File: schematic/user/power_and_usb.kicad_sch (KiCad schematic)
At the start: 27 parts, among them J1 TYPE-C-31-M-04, Q1 AO3401A, Q2 AO3401A, Q5 MBT3904DW1T1, U1 TP4056, U2 MAX17048G+T10, U3 TLV1117LV-33

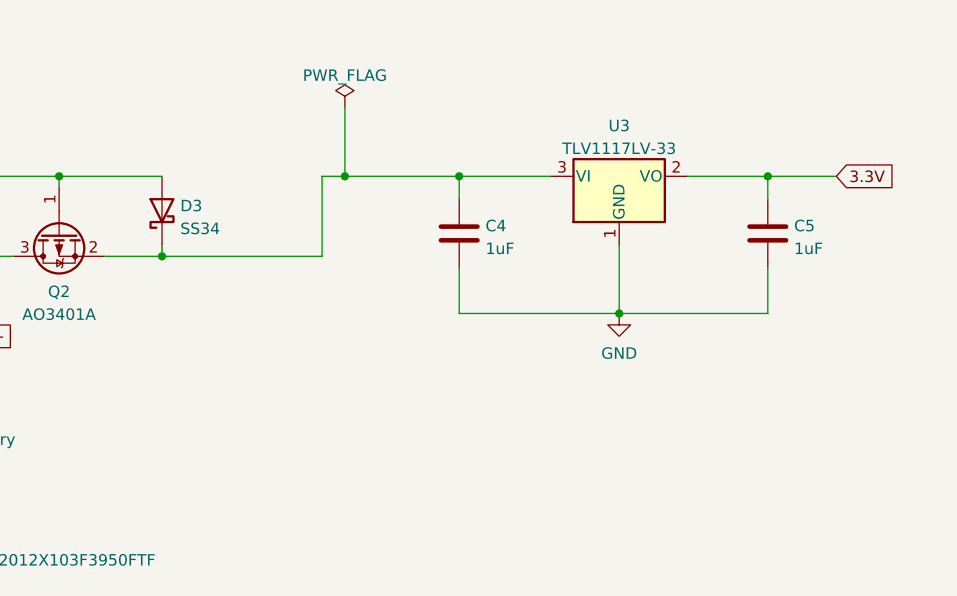
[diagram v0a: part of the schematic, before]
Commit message: v0.6 board: replace LDO with NCP167 for lower noise and Iq.
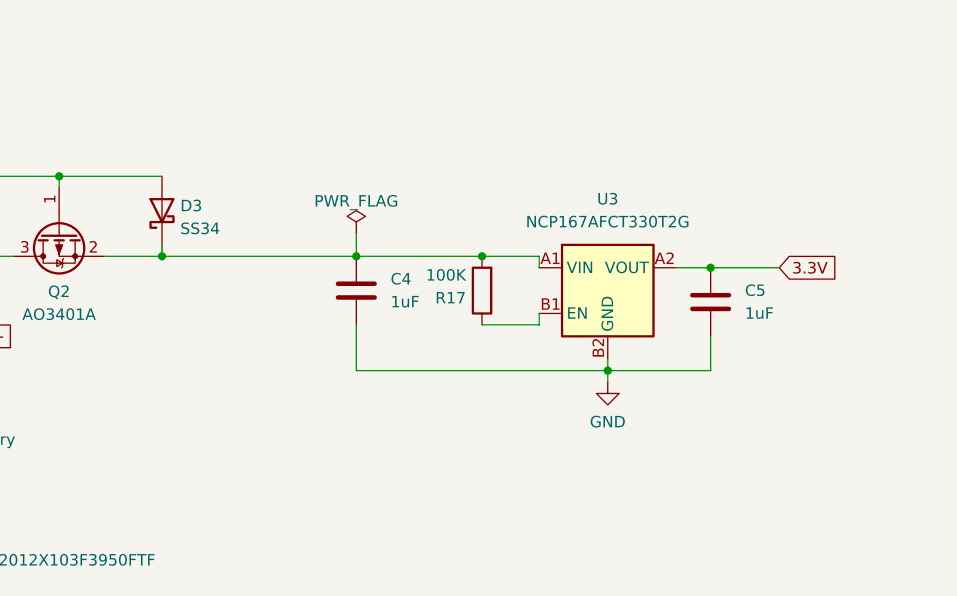
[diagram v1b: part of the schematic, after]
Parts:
- removed U3: TLV1117LV-33, Package_TO_SOT_SMD:SOT-223, symbol Regulator_Linear:TLV1117-33
- added R17: 100K, Resistor_SMD:R_0402_1005Metric, symbol Device:R
- added U3: NCP167AFCT330T2G, Package_CSP:WLCSP-4_0.64x0.64mm_P0.35mm, symbol Regulator_Linear:NCP163AFCT330T2G
- C4, C5: footprint Capacitor_SMD:C_0402_1005Metric -> Capacitor_SMD:C_0805_2012Metric; LCSC C14445 -> C28323
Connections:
- net 3.3V: now also U3.A2 (VOUT)
- net GND: now also U3.B2 (GND)
- net at C4.1, D3.1 (K), Q2.2 (S): now also R17.2, U3.A1 (VIN)
- new net: R17.1, U3.B1 (EN)

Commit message: v0.6 board: add breakouts for user and radio audio.
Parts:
- BT1: footprint TestPoint:TestPoint_2Pads_Pitch5.08mm_Drill1.3mm -> Connector_PinSocket_2.54mm:PinSocket_1x02_P2.54mm_Vertical
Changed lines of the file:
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@@
       (effects (font (size 1.27 1.27)) (justify left))
     )
-    (property "Footprint" "TestPoint:TestPoint_2Pads_Pitch5.08mm_Drill1.3mm" (id 2) (at 166.37 61.976 90)
+    (property "Footprint" "Connector_PinSocket_2.54mm:PinSocket_1x02_P2.54mm_Vertical" (id 2) (at 166.37 61.976 90)
       (effects (font (size 1.27 1.27)) hide)
     )

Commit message: v0.6 board: oops, re-associate LDO footprint.
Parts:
- U3: footprint Package_CSP:WLCSP-4_0.64x0.64mm_P0.35mm -> ezDV_production:BGA4N35P2X2_64X64X33N
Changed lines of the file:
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@@
     (property "Reference" "U3" (id 0) (at 241.3 38.1 0))
     (property "Value" "NCP167AFCT330T2G" (id 1) (at 241.3 40.64 0))
-    (property "Footprint" "Package_CSP:WLCSP-4_0.64x0.64mm_P0.35mm" (id 2) (at 241.3 48.26 0)
+    (property "Footprint" "ezDV_production:BGA4N35P2X2_64X64X33N" (id 2) (at 241.3 48.26 0)
       (effects (font (size 1.27 1.27)) hide)
     )

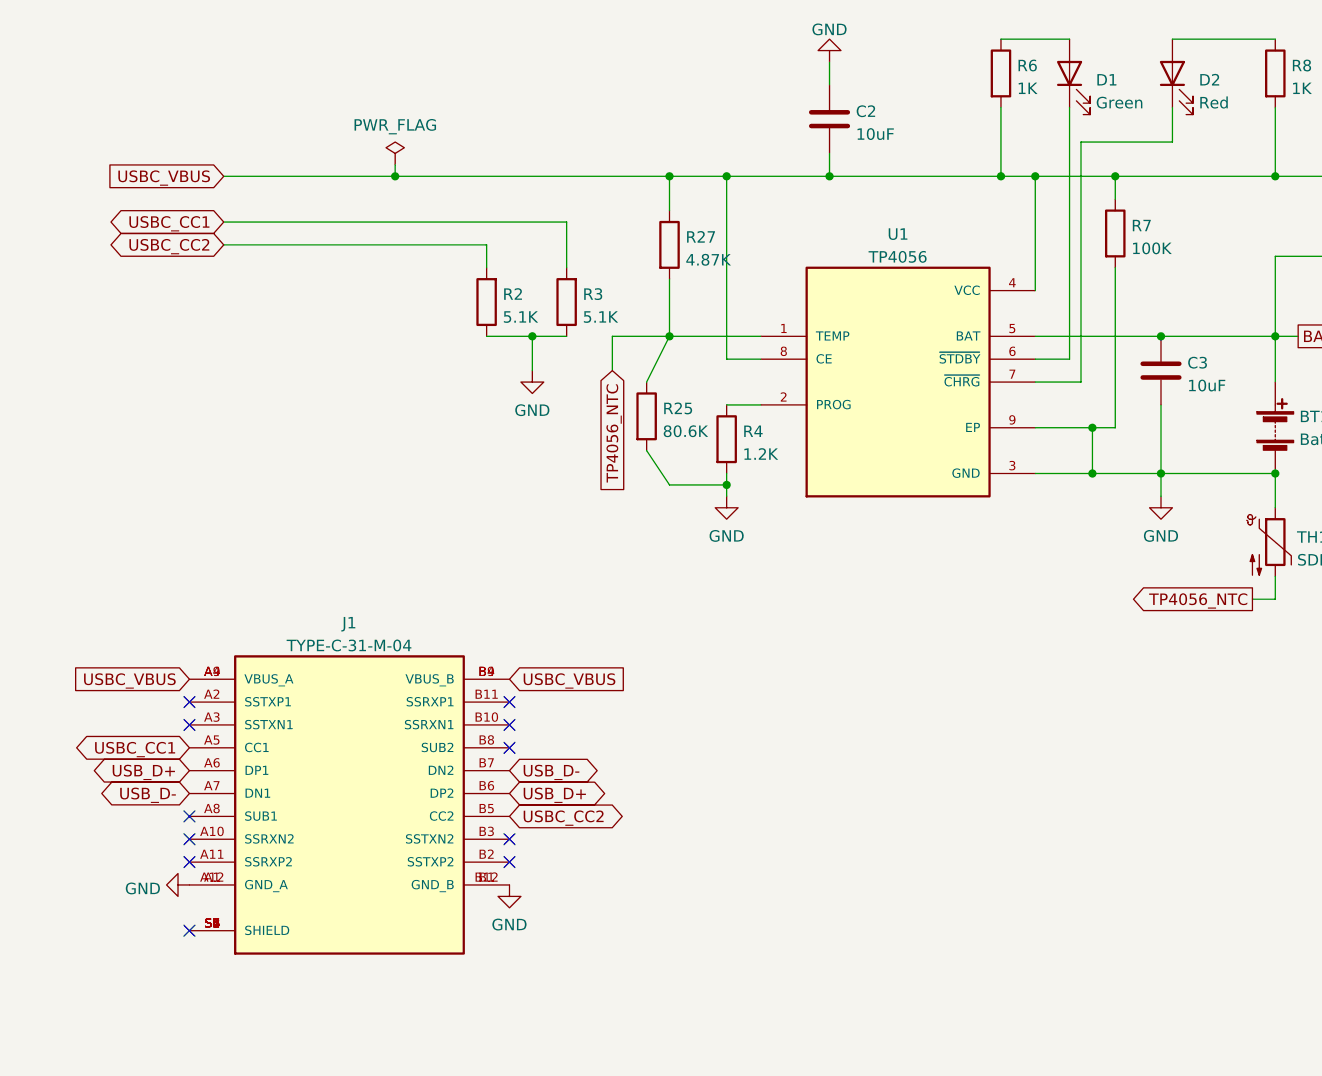
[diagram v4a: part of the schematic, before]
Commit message: v0.6 board: add protection diodes on all connectors.
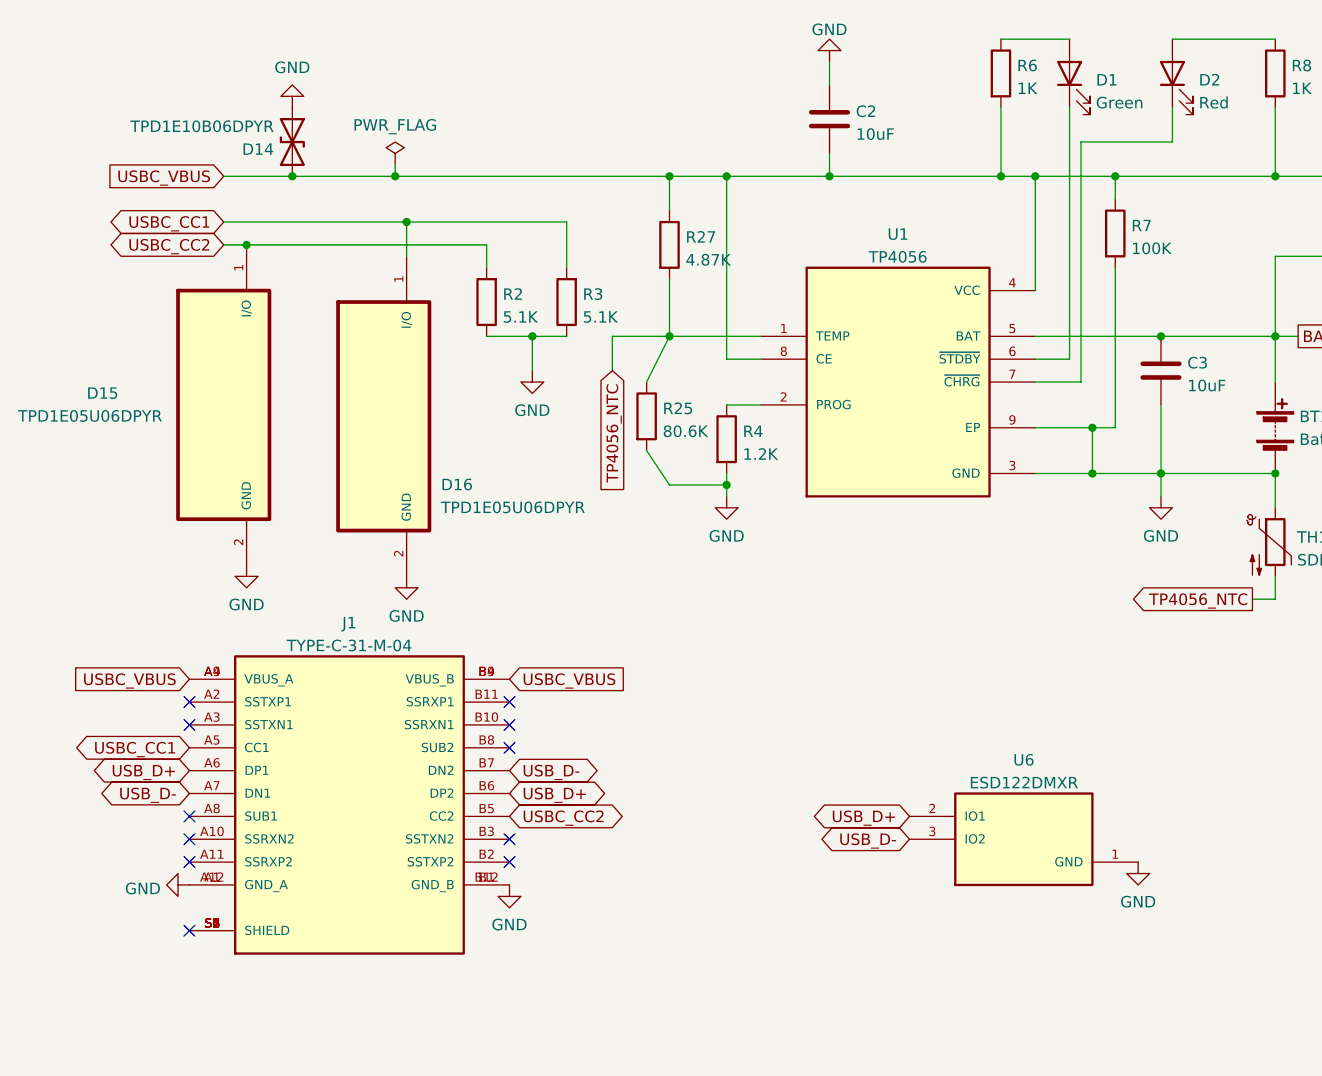
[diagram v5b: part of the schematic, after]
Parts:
- added D14: TPD1E10B06DPYR, ezDV_production:DIO_TPD1E05U06DPYR, symbol Device:D_TVS
- added D15, D16: TPD1E05U06DPYR, DIO_TPD1E05U06DPYR, symbol TPD1E05U06DPYR:TPD1E05U06DPYR
- added U6: ESD122DMXR, IC_ESD122DMXR, symbol ESD122DMXR:ESD122DMXR
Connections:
- net GND: now also D14.1 (A1), D15.2 (GND), D16.2 (GND), U6.1 (GND)
- net USBC_CC1: now also D16.1 (I/O)
- net USBC_CC2: now also D15.1 (I/O)
- net USBC_VBUS: now also D14.2 (A2)
- net USB_D+: now also U6.2 (IO1)
- net USB_D-: now also U6.3 (IO2)

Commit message: v0.7 board: re-add output LPF for audio jacks.
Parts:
- D15, D16: footprint DIO_TPD1E05U06DPYR -> ezDV_production:DIO_TPD1E05U06DPYR
- U6: footprint IC_ESD122DMXR -> ezDV_production:IC_ESD122DMXR
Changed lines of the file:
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@@
       (effects (font (size 1.27 1.27)) (justify left))
     )
-    (property "Footprint" "DIO_TPD1E05U06DPYR" (id 2) (at 67.31 62.23 0)
+    (property "Footprint" "ezDV_production:DIO_TPD1E05U06DPYR" (id 2) (at 67.31 62.23 0)
       (effects (font (size 1.27 1.27)) (justify bottom) hide)
     )
@@
     (property "Reference" "U6" (id 0) (at 138.43 100.4402 0))
     (property "Value" "ESD122DMXR" (id 1) (at 138.43 102.9771 0))
-    (property "Footprint" "IC_ESD122DMXR" (id 2) (at 138.43 109.22 0)
+    (property "Footprint" "ezDV_production:IC_ESD122DMXR" (id 2) (at 138.43 109.22 0)
       (effects (font (size 1.27 1.27)) (justify bottom) hide)
     )
@@
       (effects (font (size 1.27 1.27)) (justify left))
     )
-    (property "Footprint" "DIO_TPD1E05U06DPYR" (id 2) (at 49.53 60.96 0)
+    (property "Footprint" "ezDV_production:DIO_TPD1E05U06DPYR" (id 2) (at 49.53 60.96 0)
       (effects (font (size 1.27 1.27)) (justify bottom) hide)
     )

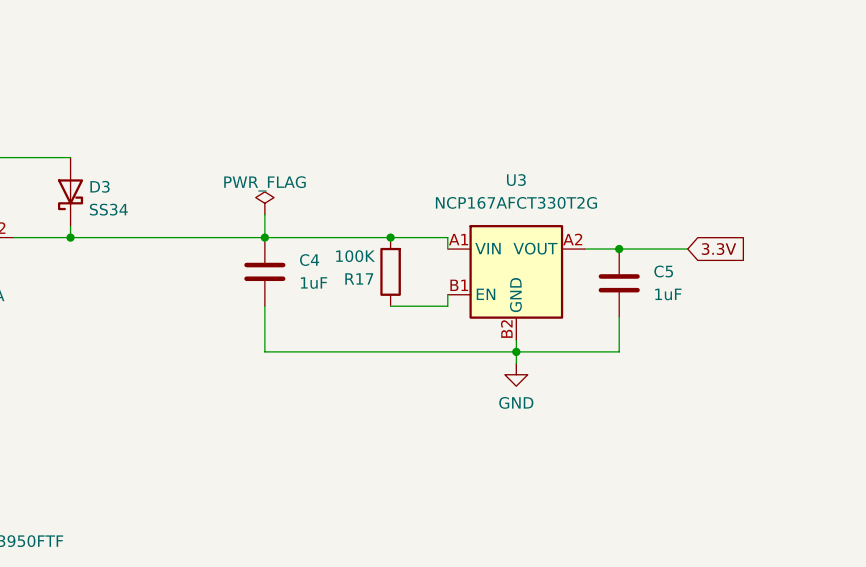
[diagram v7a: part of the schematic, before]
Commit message: v0.7 board: clarify/improve cap ratings to account for TVS diode clamp voltage.
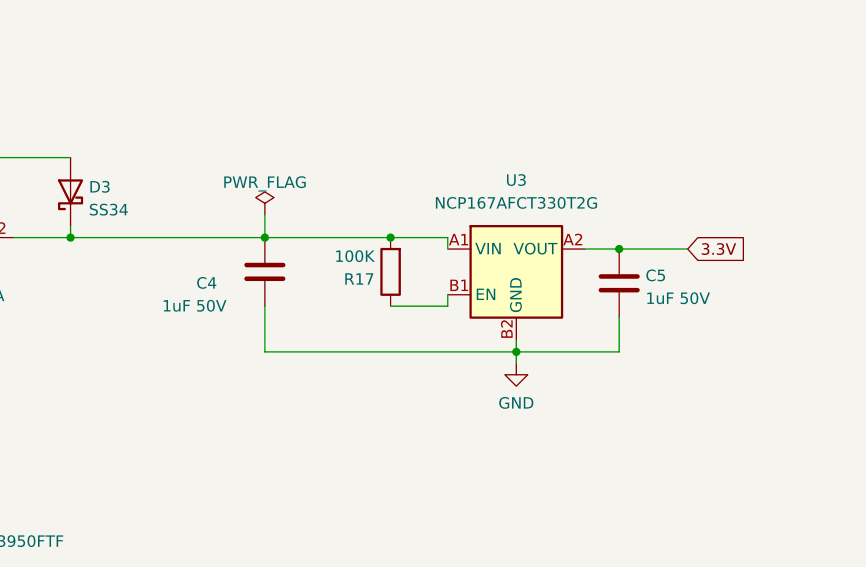
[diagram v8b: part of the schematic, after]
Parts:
- C4, C5: value 1uF -> 1uF 50V
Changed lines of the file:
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@@
   (symbol (lib_id "Device:C") (at 252.73 49.53 0) (unit 1)
     (in_bom yes) (on_board yes) (fields_autoplaced)
-    (property "Reference" "C5" (id 0) (at 256.54 48.2599 0)
-      (effects (font (size 1.27 1.27)) (justify left))
-    )
-    (property "Value" "1uF" (id 1) (at 256.54 50.7999 0)
+    (property "Reference" "C5" (id 0) (at 255.651 48.6953 0)
+      (effects (font (size 1.27 1.27)) (justify left))
+    )
+    (property "Value" "1uF 50V" (id 1) (at 255.651 51.2322 0)
       (effects (font (size 1.27 1.27)) (justify left))
     )
@@
   )
   (symbol (lib_id "Device:C") (at 213.36 48.26 0) (unit 1)
-    (in_bom yes) (on_board yes) (fields_autoplaced)
-    (property "Reference" "C4" (id 0) (at 217.17 46.9899 0)
-      (effects (font (size 1.27 1.27)) (justify left))
-    )
-    (property "Value" "1uF" (id 1) (at 217.17 49.5299 0)
-      (effects (font (size 1.27 1.27)) (justify left))
-    )
+    (in_bom yes) (on_board yes)
+    (property "Reference" "C4" (id 0) (at 205.74 49.53 0)
+      (effects (font (size 1.27 1.27)) (justify left))
+    )
+    (property "Value" "1uF 50V" (id 1) (at 201.93 52.07 0)
+      (effects (font (size 1.27 1.27)) (justify left))
+    )
